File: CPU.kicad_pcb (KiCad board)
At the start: 4 copper layers, 212 parts, among them J1 Conn_02x36_Odd_Even, P10 Conn_02x08_Counter_Clockwise, P2 Conn_02x13_Top_Bottom, P3 Conn_02x13_Top_Bottom, P4 Conn_02x08_Counter_Clockwise, P5 Conn_02x25_Counter_Clockwise, P6 Conn_02x25_Counter_Clockwise, P7 Conn_02x07_Counter_Clockwise, P8 Conn_02x08_Counter_Clockwise

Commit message: Fix board outline
Non-duplicating designators for hole and proper layer for 4th edge
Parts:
- renumbered REF** to HOLE1, REF** to HOLE2, REF** to HOLE3, REF** to HOLE4
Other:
- board outline added: 355 x 203 mm
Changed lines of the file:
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@@
     (descr "Mounting Hole 2.5mm, no annular")
     (tags "mounting hole 2.5mm no annular")
-    (attr exclude_from_pos_files exclude_from_bom)
-    (fp_text reference "REF**" (at 0 -3.5) (layer "F.SilkS") hide
+    (attr board_only exclude_from_pos_files exclude_from_bom)
+    (fp_text reference "HOLE4" (at 0 -3.5) (layer "F.SilkS") hide
       (effects (font (size 1 1) (thickness 0.15)))
     )
-    (fp_text value "MountingHole_2.5mm" (at 0 3.5) (layer "F.Fab")
+    (fp_text value "MountingHole_2.5mm" (at 0 3.5) (layer "F.Fab") hide
       (effects (font (size 1 1) (thickness 0.15)))
     )
@@
     (descr "Mounting Hole 2.5mm, no annular")
     (tags "mounting hole 2.5mm no annular")
-    (attr exclude_from_pos_files exclude_from_bom)
-    (fp_text reference "REF**" (at 0 -3.5) (layer "F.SilkS") hide
+    (attr board_only exclude_from_pos_files exclude_from_bom)
+    (fp_text reference "HOLE2" (at 0 -3.5) (layer "F.SilkS") hide
       (effects (font (size 1 1) (thickness 0.15)))
     )
@@
     (descr "Mounting Hole 2.5mm, no annular")
     (tags "mounting hole 2.5mm no annular")
-    (attr exclude_from_pos_files exclude_from_bom)
-    (fp_text reference "REF**" (at 0 -3.5) (layer "F.SilkS") hide
+    (attr board_only exclude_from_pos_files exclude_from_bom)
+    (fp_text reference "HOLE1" (at 0 -3.5) (layer "F.SilkS") hide
       (effects (font (size 1 1) (thickness 0.15)))
     )
@@
     (descr "Mounting Hole 2.5mm, no annular")
     (tags "mounting hole 2.5mm no annular")
-    (attr exclude_from_pos_files exclude_from_bom)
-    (fp_text reference "REF**" (at 0 -3.5) (layer "F.SilkS") hide
+    (attr board_only exclude_from_pos_files exclude_from_bom)
+    (fp_text reference "HOLE3" (at 0 -3.5) (layer "F.SilkS") hide
       (effects (font (size 1 1) (thickness 0.15)))
     )
@@
   )
   (gr_line (start 38.5 26) (end 26 38.5) (layer "F.SilkS") (width 0.15))
+  (gr_rect (start 24 24) (end 379 227) (layer "Edge.Cuts") (width 0.1) (fill none))
   (gr_rect (start 24 220.5) (end 30.5 227) (layer "User.1") (width 0.15) (fill none))
   (gr_rect (start 372.5 220.5) (end 379 227) (layer "User.1") (width 0.15) (fill none))
   (gr_rect (start 372.5 24) (end 379 30.5) (layer "User.1") (width 0.15) (fill none))
   (gr_rect (start 24 24) (end 30.5 30.5) (layer "User.1") (width 0.15) (fill none))
-  (gr_rect (start 24 24) (end 379 227) (layer "User.1") (width 0.1) (fill none))
   (gr_text "TOP" (at 56.165 29.275) (layer "F.SilkS")
     (effects (font (size 2 2) (thickness 0.5)))

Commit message: Manual layout WIP
Attempt on manually-assisted layout. This uncovers some opportunities for
optimization.
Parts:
- U_BH13, U_BL13: value 93427С -> 93427C
- moved P8 24.1 mm to (238.8, 35.6), turned to 90 degrees
- moved U_A7 14.0 mm to (351.8, 95.3)
- moved U_A6 13.7 mm to (340.4, 111.8), turned to 90 degrees
- moved C45 13.0 mm to (327.7, 109.2)
- moved C46 3.59 mm to (320.0, 109.2)
- moved U_B6 1.25 mm to (320.0, 95.3)
- turned U_F5 to 90 degrees
- turned U_H5 to 90 degrees
- turned U_J5 to 90 degrees
- turned U_K5 to 90 degrees
- turned U_L5 to 90 degrees
- turned U_M5 to 90 degrees
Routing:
- net +5V: track 0.00 -> 178.5 mm
- net MWS.A_{7}: track 0.00 -> 173.2 mm
- net MWS.A_{6}: track 0.00 -> 173.0 mm
- net MWS.A_{8}: track 0.00 -> 58.4 mm
- net MWS.A_{5}: track 0.00 -> 57.8 mm
- net MWS.A_{9}: track 0.00 -> 29.4 mm
- net MWS.A_{0}: track 0.00 -> 29.1 mm
- net Net-(R10-Pad2): track 0.00 -> 29.0 mm
- net GND: track 0.00 -> 29.0 mm
- net MWS.A_{2}: track 0.00 -> 29.0 mm
- net /P7_14: track 0.00 -> 29.0 mm
- net MWS.A_{1}: track 0.00 -> 29.0 mm
- net MWS.A_{4}: track 0.00 -> 28.9 mm
- net MWS.A_{3}: track 0.00 -> 28.9 mm
- net MWS.A_{10}: track 0.00 -> 28.8 mm

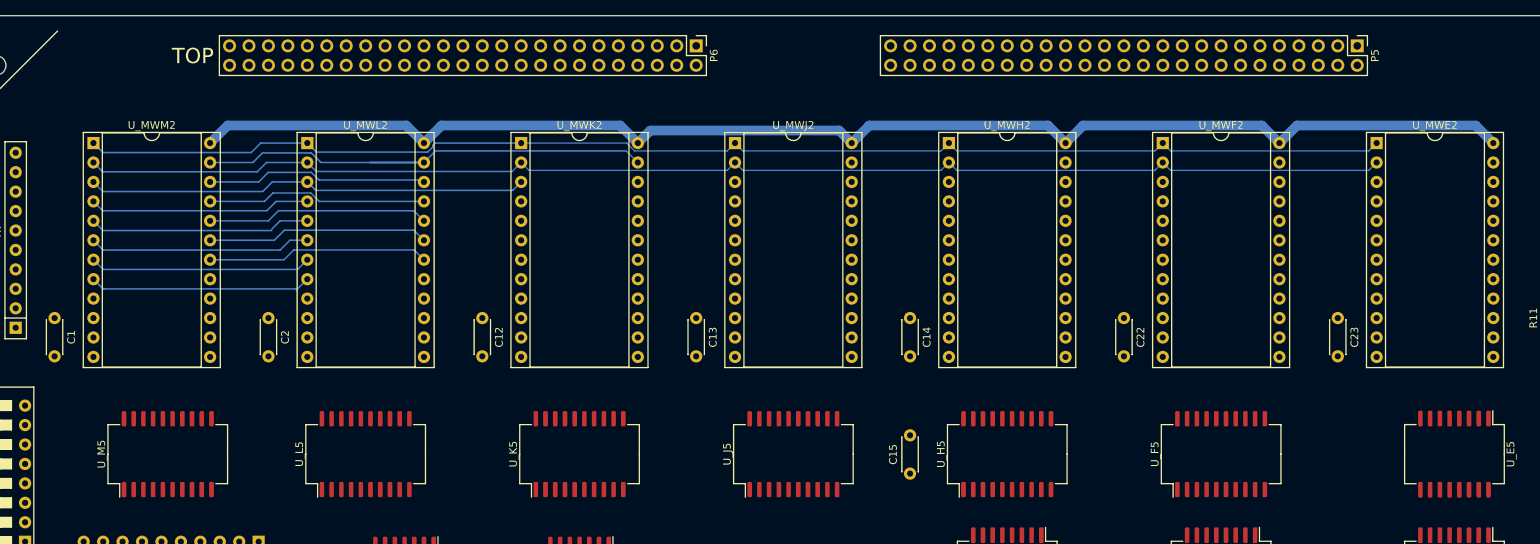
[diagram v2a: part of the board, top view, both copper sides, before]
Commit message: uCode address lines routed
PoC version with different line twist for U_M5
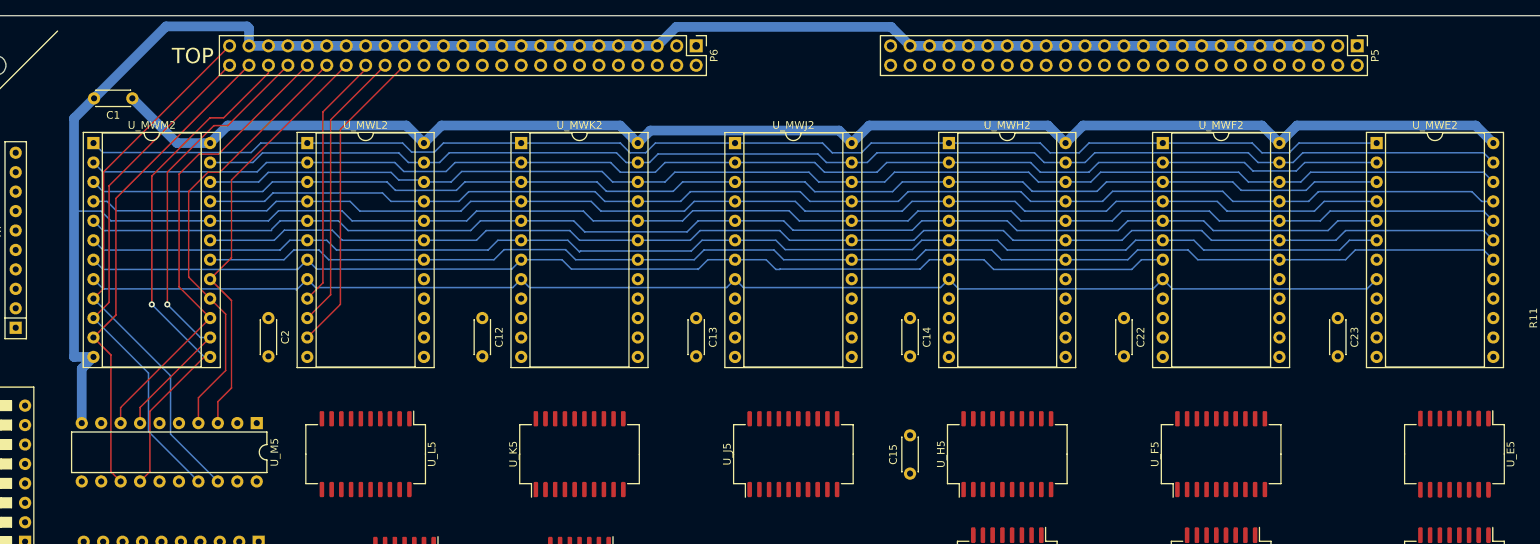
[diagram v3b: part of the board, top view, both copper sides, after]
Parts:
- U_M5: footprint Package_SO:SOIC-20W_7.5x15.4mm_P1.27mm -> Package_DIP:DIP-20_W7.62mm
- moved C1 30.4 mm to (48.3, 34.8), turned to 180 degrees
- moved U_M5 12.3 mm to (64.5, 77.2), turned to -90 degrees
- turned U_L5 to -90 degrees
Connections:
- U_M5 pad 12: MW.E2_{4} -> MW.E2_{2}
- U_M5 pad 13: /MWR.E2_{4} -> /MWR.E2_{2}
- U_M5 pad 14: /MWR.E2_{5} -> /MWR.E2_{3}
- U_M5 pad 15: MW.E2_{5} -> MW.E2_{3}
- U_M5 pad 6: MW.E2_{2} -> MW.E2_{4}
- U_M5 pad 7: /MWR.E2_{2} -> /MWR.E2_{4}
- U_M5 pad 8: /MWR.E2_{3} -> /MWR.E2_{5}
- U_M5 pad 9: MW.E2_{3} -> MW.E2_{5}
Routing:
- net GND: track 29.0 -> 407.3 mm
- net MWS.A_{2}: track 29.0 -> 174.1 mm
- net MWS.A_{3}: track 28.9 -> 174.0 mm
- net MWS.A_{9}: track 29.4 -> 174.4 mm
- net /P7_14: track 29.0 -> 174.0 mm
- net MWS.A_{10}: track 28.8 -> 173.8 mm
- net Net-(R10-Pad2): track 29.0 -> 174.0 mm
- net MWS.A_{4}: track 28.9 -> 173.9 mm
- net MWS.A_{0}: track 29.1 -> 173.6 mm
- net MWS.A_{1}: track 29.0 -> 144.9 mm
- net MWS.A_{5}: track 57.8 -> 173.6 mm
- net MWS.A_{8}: track 58.4 -> 174.1 mm
- net /MWR.E2_{0}: track 0.00 -> 71.0 mm
- net /MWR.E2_{3}: track 0.00 -> 69.6 mm, vias 0 -> 1
- net /MWR.E2_{1}: track 0.00 -> 67.4 mm
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
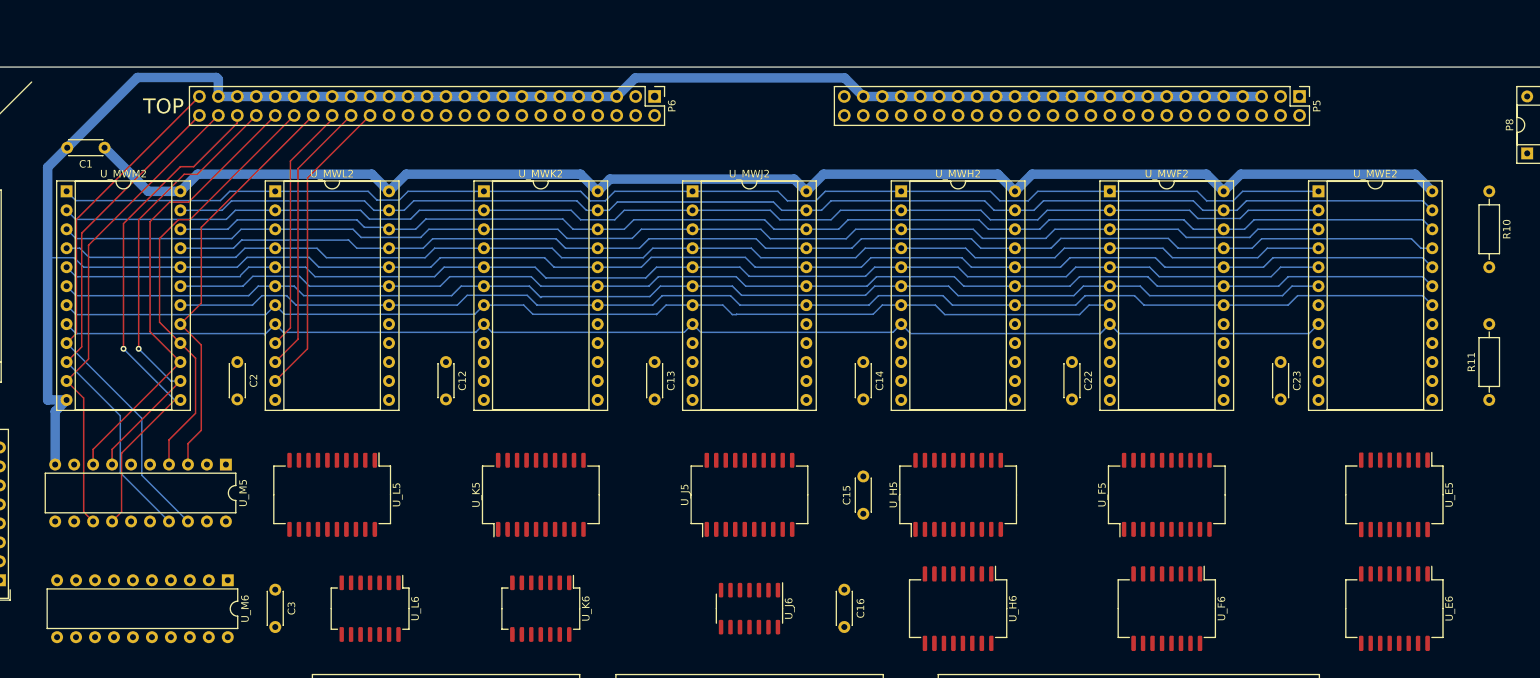
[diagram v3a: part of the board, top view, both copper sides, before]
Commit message: Routing WIP
MWM2, MWL2 with their buffers.

From this point it makes sense to play with the layout and move some chips
around, so this is the checkpoint.
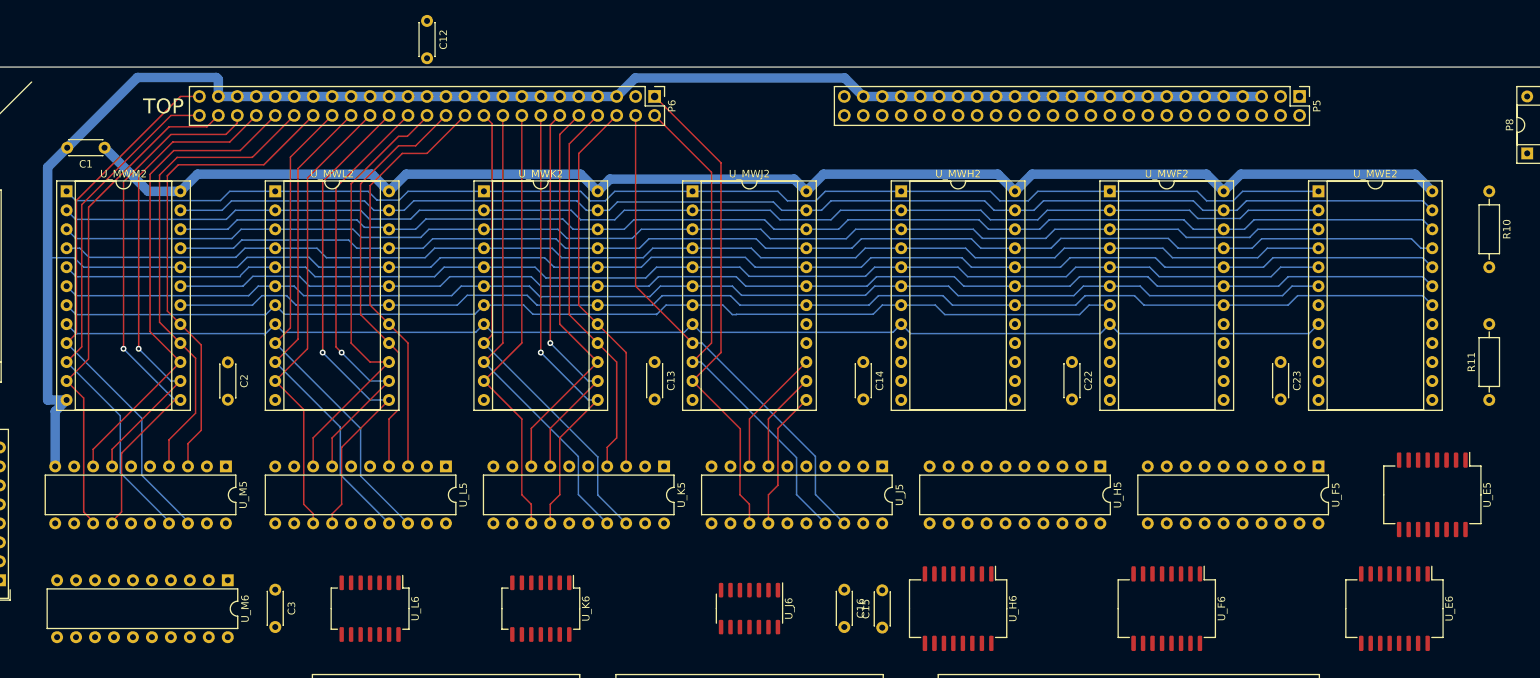
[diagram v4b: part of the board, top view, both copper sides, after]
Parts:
- U_F5, U_H5, U_J5, U_K5, U_L5: footprint Package_SO:SOIC-20W_7.5x15.4mm_P1.27mm -> Package_DIP:DIP-20_W7.62mm
- moved C12 45.8 mm to (91.4, 17.8)
- moved U_F5 20.7 mm to (210.8, 77.5), turned to -90 degrees
- moved U_H5 19.4 mm to (181.6, 77.5), turned to -90 degrees
- moved U_J5 18.2 mm to (152.4, 77.5), turned to -90 degrees
- moved U_K5 16.9 mm to (123.2, 77.5), turned to -90 degrees
- moved U_L5 15.7 mm to (94.0, 77.5)
- moved C15 15.5 mm to (152.4, 99.1)
- moved U_E5 5.08 mm to (226.1, 81.3)
- moved C2 1.27 mm to (64.8, 63.5)
- moved U_M5 0.25 mm to (64.5, 77.5)
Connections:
- U_F5 pad 12: MW.B5_{4} -> MW.B5_{2}
- U_F5 pad 13: /MWR.B5_{4} -> /MWR.B5_{2}
- U_F5 pad 14: /MWR.B5_{5} -> /MWR.B5_{3}
- U_F5 pad 15: MW.B5_{5} -> MW.B5_{3}
- U_F5 pad 6: MW.B5_{2} -> MW.B5_{4}
- U_F5 pad 7: /MWR.B5_{2} -> /MWR.B5_{4}
- U_F5 pad 8: /MWR.B5_{3} -> /MWR.B5_{5}
- U_F5 pad 9: MW.B5_{3} -> MW.B5_{5}
- U_H5 pad 12: MW.C4_{4} -> MW.C4_{2}
- U_H5 pad 13: /MWR.C4_{4} -> /MWR.C4_{2}
- U_H5 pad 14: /MWR.C4_{5} -> /MWR.C4_{3}
- U_H5 pad 15: MW.C4_{5} -> MW.C4_{3}
- U_H5 pad 6: MW.C4_{2} -> MW.C4_{4}
- U_H5 pad 7: /MWR.C4_{2} -> /MWR.C4_{4}
- U_H5 pad 8: /MWR.C4_{3} -> /MWR.C4_{5}
- U_H5 pad 9: MW.C4_{3} -> MW.C4_{5}
- U_J5 pad 12: MW.F1_{4} -> MW.F1_{2}
- U_J5 pad 13: /MWR.F1_{4} -> /MWR.F1_{2}
- U_J5 pad 14: /MWR.F1_{5} -> /MWR.F1_{3}
- U_J5 pad 15: MW.F1_{5} -> MW.F1_{3}
- U_J5 pad 6: MW.F1_{2} -> MW.F1_{4}
- U_J5 pad 7: /MWR.F1_{2} -> /MWR.F1_{4}
- U_J5 pad 8: /MWR.F1_{3} -> /MWR.F1_{5}
- U_J5 pad 9: MW.F1_{3} -> MW.F1_{5}
- U_K5 pad 12: MW.A6_{4} -> MW.A6_{2}
- U_K5 pad 13: /MWR.A6_{4} -> /MWR.A6_{2}
- U_K5 pad 14: /MWR.A6_{5} -> /MWR.A6_{3}
- U_K5 pad 15: MW.A6_{5} -> MW.A6_{3}
- U_K5 pad 6: MW.A6_{2} -> MW.A6_{4}
- U_K5 pad 7: /MWR.A6_{2} -> /MWR.A6_{4}
- U_K5 pad 8: /MWR.A6_{3} -> /MWR.A6_{5}
- U_K5 pad 9: MW.A6_{3} -> MW.A6_{5}
- U_L5 pad 12: MW.D3_{4} -> MW.D3_{2}
- U_L5 pad 13: /MWR.D3_{4} -> /MWR.D3_{2}
- U_L5 pad 14: /MWR.D3_{5} -> /MWR.D3_{3}
- U_L5 pad 15: MW.D3_{5} -> MW.D3_{3}
- U_L5 pad 6: MW.D3_{2} -> MW.D3_{4}
- U_L5 pad 7: /MWR.D3_{2} -> /MWR.D3_{4}
- U_L5 pad 8: /MWR.D3_{3} -> /MWR.D3_{5}
- U_L5 pad 9: MW.D3_{3} -> MW.D3_{5}
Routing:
- net /MWR.F1_{0}: track 0.00 -> 66.9 mm
- net /MWR.F1_{1}: track 0.00 -> 66.9 mm
- net /MWR.D3_{3}: track 0.00 -> 66.6 mm, vias 0 -> 1
- net /MWR.F1_{2}: track 0.00 -> 65.6 mm
- net /MWR.A6_{0}: track 0.00 -> 63.4 mm
- net /MWR.A6_{1}: track 0.00 -> 62.5 mm
- net /MWR.A6_{3}: track 0.00 -> 61.1 mm, vias 0 -> 1
- net /MWR.D3_{5}: track 0.00 -> 59.7 mm
- net /MWR.A6_{2}: track 0.00 -> 59.4 mm
- net /MWR.D3_{4}: track 0.00 -> 58.6 mm, vias 0 -> 1
- net /MWR.D3_{7}: track 0.00 -> 56.3 mm
- net /MWR.D3_{6}: track 0.00 -> 55.7 mm
- net /MWR.A6_{5}: track 0.00 -> 53.8 mm
- net /MWR.A6_{4}: track 0.00 -> 53.5 mm, vias 0 -> 1
- net /MWR.A6_{6}: track 0.00 -> 51.7 mm
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
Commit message: Routing WIP
A checkpoint for possble restoring. I don't like microcode lines going back and
forth, looks like swapping chips wasn't a good idea.
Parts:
- DSW1: footprint Button_Switch_THT:SW_DIP_SPSTx08_Slide_9.78x22.5mm_W7.62mm_P2.54mm -> Button_Switch_THT:SW_DIP_SPSTx08_Piano_10.8x21.88mm_W7.62mm_P2.54mm
- U_D2, U_F6, U_H6, U_M13, U_M9: footprint Package_SO:SOIC-16W_7.5x12.8mm_P1.27mm -> Package_DIP:DIP-16_W7.62mm
- U_J9: footprint Package_SO:SOIC-20W_7.5x15.4mm_P1.27mm -> Package_DIP:DIP-20_W7.62mm
- U_K6, U_L6: footprint Package_SO:SO-14_5.3x10.2mm_P1.27mm -> Package_DIP:DIP-14_W7.62mm
- U_K9: footprint Package_SO:SO-16_5.3x10.2mm_P1.27mm -> Package_DIP:DIP-16_W7.62mm
- XTAL1: footprint Crystal:Crystal_HC52-U_Horizontal -> Crystal:Crystal_HC18-U_Vertical
- moved R7 91.1 mm to (-12.7, 143.5), turned to -90 degrees
- moved C16 81.0 mm to (123.1, 16.7)
- moved C15 79.6 mm to (131.7, 22.2)
- moved U_J6 70.9 mm to (191.8, 138.4)
- moved C4 65.4 mm to (5.84, 113.3)
- moved U_F6 62.3 mm to (130.8, 114.3), turned to 0 degrees
- moved R11 56.8 mm to (223.5, 12.7), turned to -90 degrees
- moved U_H6 49.1 mm to (116.8, 114.3), turned to 0 degrees
- moved C12 46.1 mm to (94.5, 63.8)
- moved R8 45.0 mm to (95.2, 158.8), turned to 90 degrees
- moved U_K6 41.4 mm to (114.3, 137.2)
- moved U_L6 41.3 mm to (91.4, 137.2)
- moved R4 41.3 mm to (-5.08, 137.9)
- moved R5 34.9 mm to (170.2, 141.0)
- moved C1 30.9 mm to (36.8, 63.5), turned to -90 degrees
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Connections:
- DSW1 pad 1: /Sys.Reset -> GND
- DSW1 pad 10: GND -> /SW_I
- DSW1 pad 11: GND -> /SW_H
- DSW1 pad 12: GND -> /SW_R
- DSW1 pad 13: GND -> /SW_1
- DSW1 pad 14: GND -> /SW_2
- DSW1 pad 15: GND -> /SW_3
- DSW1 pad 16: GND -> /Sys.Reset
- DSW1 pad 2: /SW_3 -> GND
- DSW1 pad 3: /SW_2 -> GND
- DSW1 pad 4: /SW_1 -> GND
- DSW1 pad 5: /SW_R -> GND
- DSW1 pad 6: /SW_H -> GND
- DSW1 pad 7: /SW_I -> GND
- DSW1 pad 8: /SW_O -> GND
- DSW1 pad 9: GND -> /SW_O
- P7 pad 14: /P7_14 -> unconnected-(P7-Pad14)
- R11 pad 2: /P7_14 -> Net-(R11-Pad2)
- U_M6 pad 11: MW.E2_{3} -> MW.E2_{2}
- U_M6 pad 12: DataP.D_{7} -> DataP.D_{5}
- U_M6 pad 13: MW.E2_{2} -> MW.E2_{3}
- U_M6 pad 14: DataP.D_{6} -> DataP.D_{4}
- U_M6 pad 16: DataP.D_{5} -> DataP.D_{6}
- U_M6 pad 18: DataP.D_{4} -> DataP.D_{7}
- U_M6 pad 2: MW.E2_{4} -> MW.E2_{7}
- U_M6 pad 4: MW.E2_{5} -> MW.E2_{6}
- U_M6 pad 6: MW.E2_{6} -> MW.E2_{4}
- U_M6 pad 7: DataP.D_{2} -> DataP.D_{3}
- U_M6 pad 8: MW.E2_{7} -> MW.E2_{5}
- U_M6 pad 9: DataP.D_{3} -> DataP.D_{2}
- U_M7 pad 11: /SW_1 -> /SW_3
- U_M7 pad 12: DataP.D_{0} -> DataP.D_{2}
- U_M7 pad 13: /SW_2 -> /~{FPC_SW_4}
- U_M7 pad 14: DataP.D_{1} -> DataP.D_{3}
- U_M7 pad 15: /SW_3 -> /SW_2
- U_M7 pad 16: DataP.D_{2} -> DataP.D_{1}
- U_M7 pad 17: /~{FPC_SW_4} -> /SW_1
- U_M7 pad 18: DataP.D_{3} -> DataP.D_{0}
- U_M7 pad 2: /SW_R -> /~{RT_INT}
- U_M7 pad 3: DataP.D_{3} -> DataP.D_{0}
- U_M7 pad 4: /SW_H -> /SW_I
- U_M7 pad 5: DataP.D_{2} -> DataP.D_{1}
- U_M7 pad 6: /SW_I -> /SW_R
- U_M7 pad 7: DataP.D_{1} -> DataP.D_{3}
- U_M7 pad 8: /~{RT_INT} -> /SW_H
- U_M7 pad 9: DataP.D_{0} -> DataP.D_{2}
- U_MWE2 pad 18: /P7_14 -> Net-(R11-Pad2)
- U_MWF2 pad 18: /P7_14 -> Net-(R11-Pad2)
- U_MWH2 pad 18: /P7_14 -> Net-(R11-Pad2)
- U_MWJ2 pad 18: /P7_14 -> Net-(R11-Pad2)
- U_MWK2 pad 18: /P7_14 -> Net-(R11-Pad2)
- U_MWL2 pad 18: /P7_14 -> Net-(R11-Pad2)
- U_MWM2 pad 18: /P7_14 -> Net-(R11-Pad2)
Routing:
- net GND: track 407.3 -> 769.0 mm
- net +5V: track 191.1 -> 410.8 mm
- net MW.A6_{7}: track 0.00 -> 176.2 mm, vias 0 -> 1
- net Net-(R11-Pad2): track 0.00 -> 174.0 mm
- net /P7_14: track 174.0 -> 0.00 mm
- net MW.A6_{5}: track 0.00 -> 163.3 mm, vias 0 -> 1
- net /~{ClockB_{0}}: track 0.00 -> 147.4 mm, vias 0 -> 1
- net DataP.D_{4}: track 0.00 -> 129.3 mm
- net DataP.D_{5}: track 0.00 -> 126.4 mm, vias 0 -> 1
- net Net-(R8-Pad2): track 0.00 -> 122.3 mm, vias 0 -> 1
- net DataP.D_{6}: track 0.00 -> 118.3 mm
- net MW.E2_{3}: track 0.00 -> 116.8 mm, vias 0 -> 1
- net MW.E2_{2}: track 0.00 -> 111.2 mm
- net MW.A6_{2}: track 0.00 -> 111.2 mm, vias 0 -> 1
- net MWS.A_{8}: track 174.1 -> 282.3 mm, vias 0 -> 1
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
